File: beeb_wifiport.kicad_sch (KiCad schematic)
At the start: 18 parts, among them J1 User Port, J2 USB4105-GF-A, J3 1040310811, SW1 EVQ-P7A01P, SW2 EVQ-P7A01P, U1 ESP32-S3-MINI-1, U3 LDL212PV33R, U4 NXB0104GU12

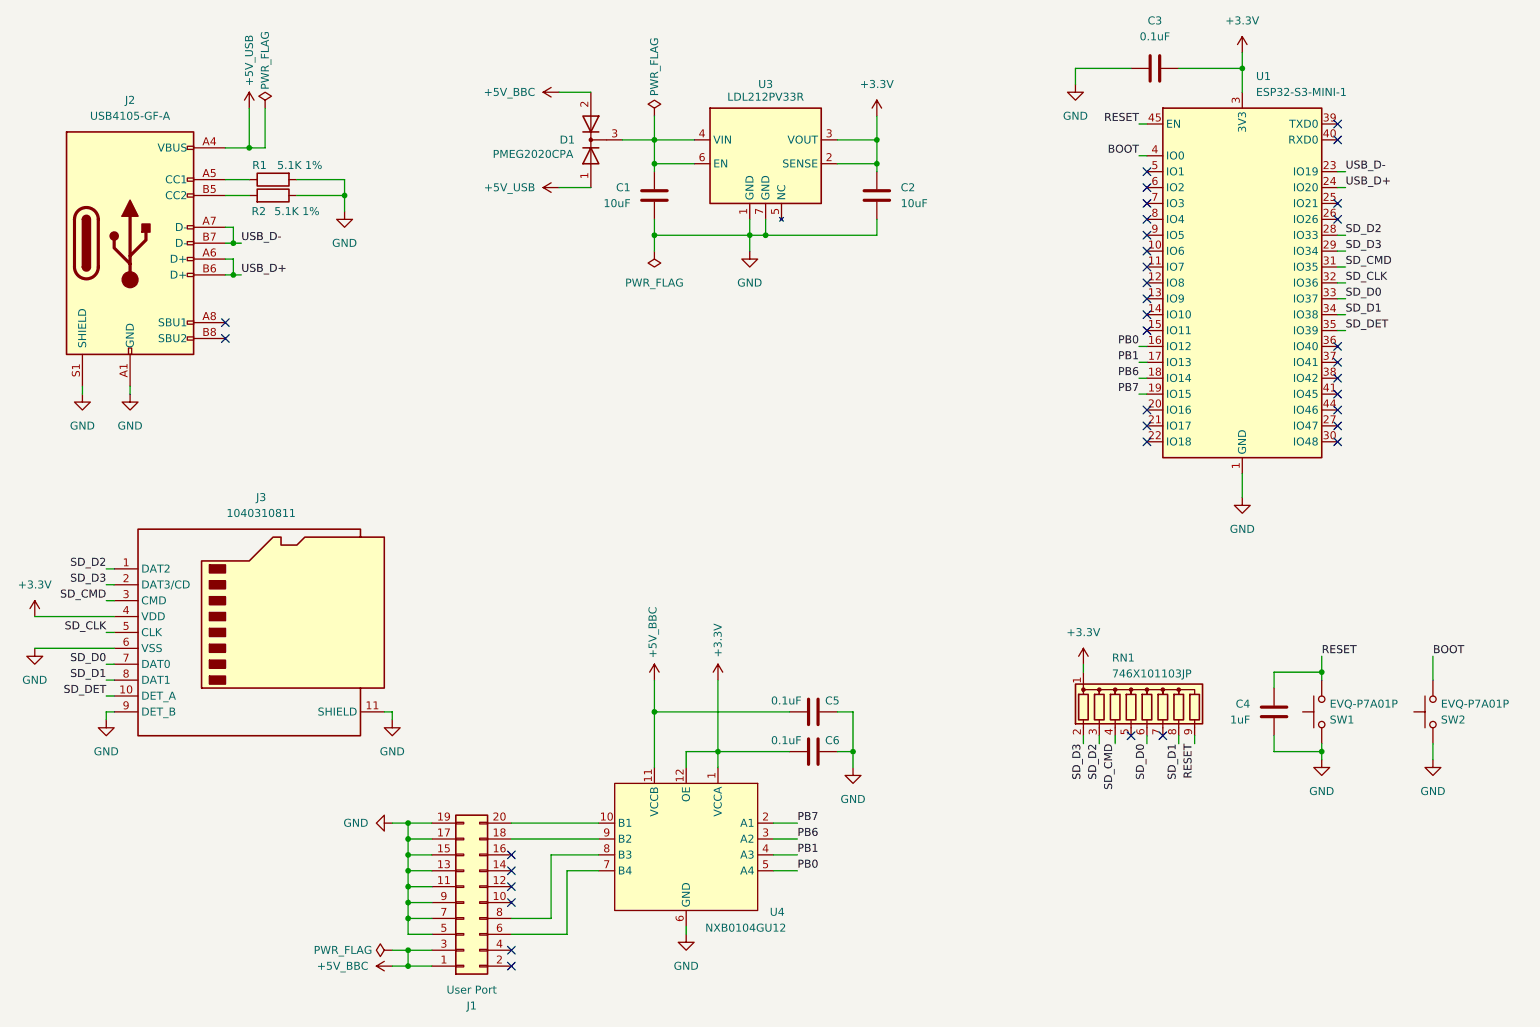
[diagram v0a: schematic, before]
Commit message: Clarify part numbers
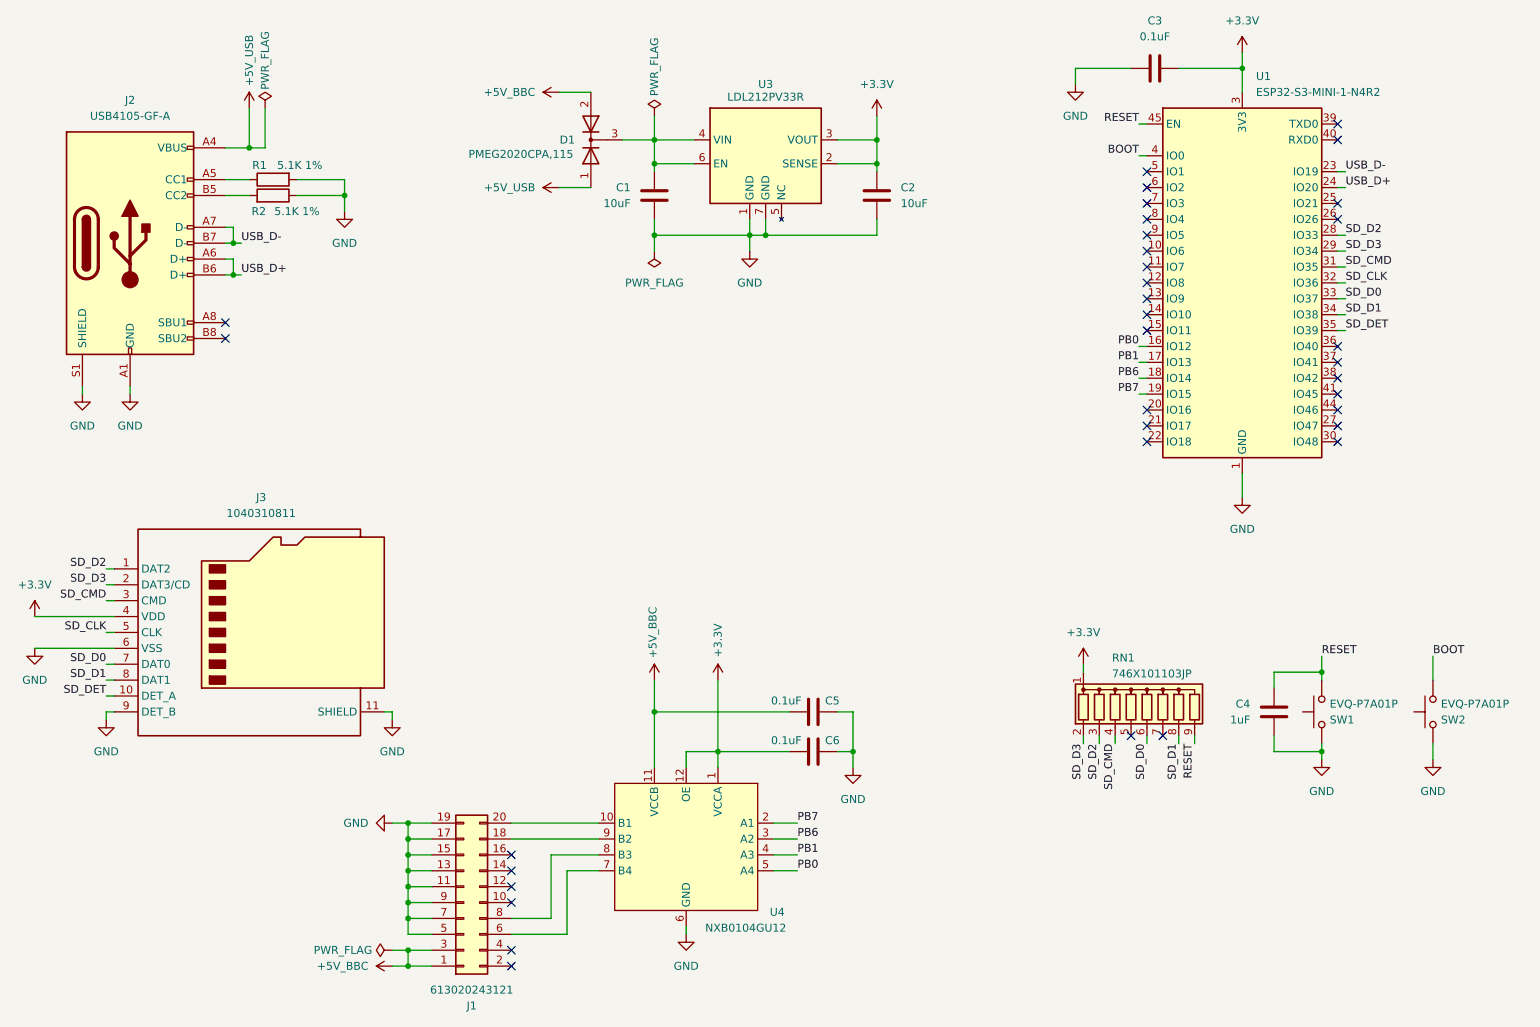
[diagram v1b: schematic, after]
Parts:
- D1: value PMEG2020CPA -> PMEG2020CPA,115
- J1: value User Port -> 613020243121
- U1: value ESP32-S3-MINI-1 -> ESP32-S3-MINI-1-N4R2
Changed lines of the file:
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@@
 			)
 		)
-		(property "Value" "ESP32-S3-MINI-1"
+		(property "Value" "ESP32-S3-MINI-1-N4R2"
 			(at 226.9841 39.37 0)
 			(effects
@@
 			)
 		)
-		(property "Value" "User Port"
+		(property "Value" "613020243121"
 			(at 101.6 182.88 0)
 			(effects
@@
 			)
 		)
-		(property "Value" "PMEG2020CPA"
+		(property "Value" "PMEG2020CPA,115"
 			(at 117.856 49.276 90)
 			(effects
